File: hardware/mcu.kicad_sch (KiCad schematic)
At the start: 22 parts, among them SW301 RESET, U301 STM32G431

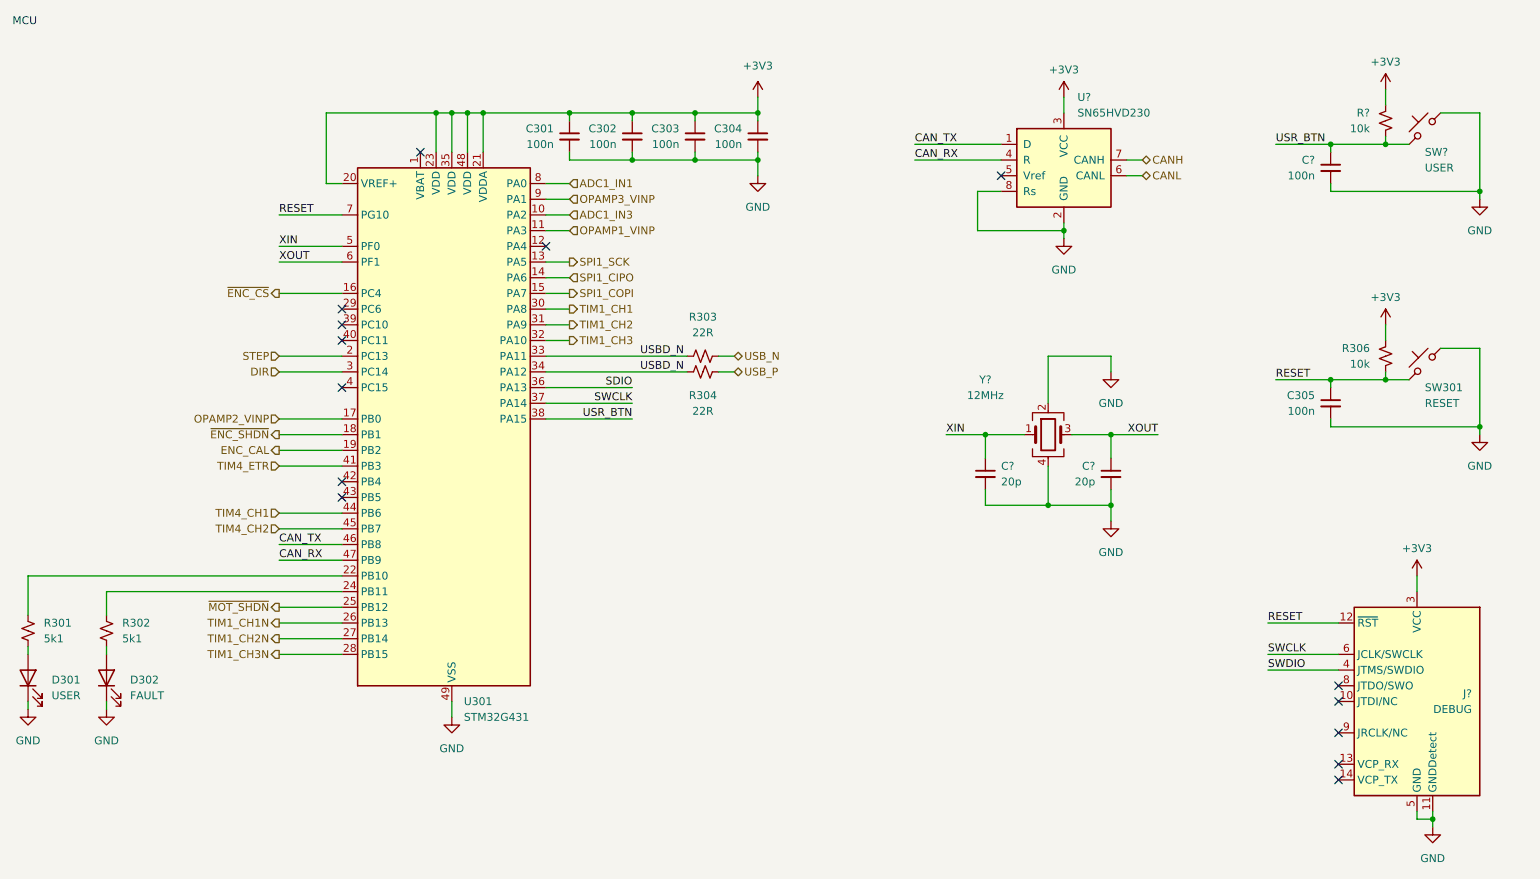
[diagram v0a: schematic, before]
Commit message: finish component selection
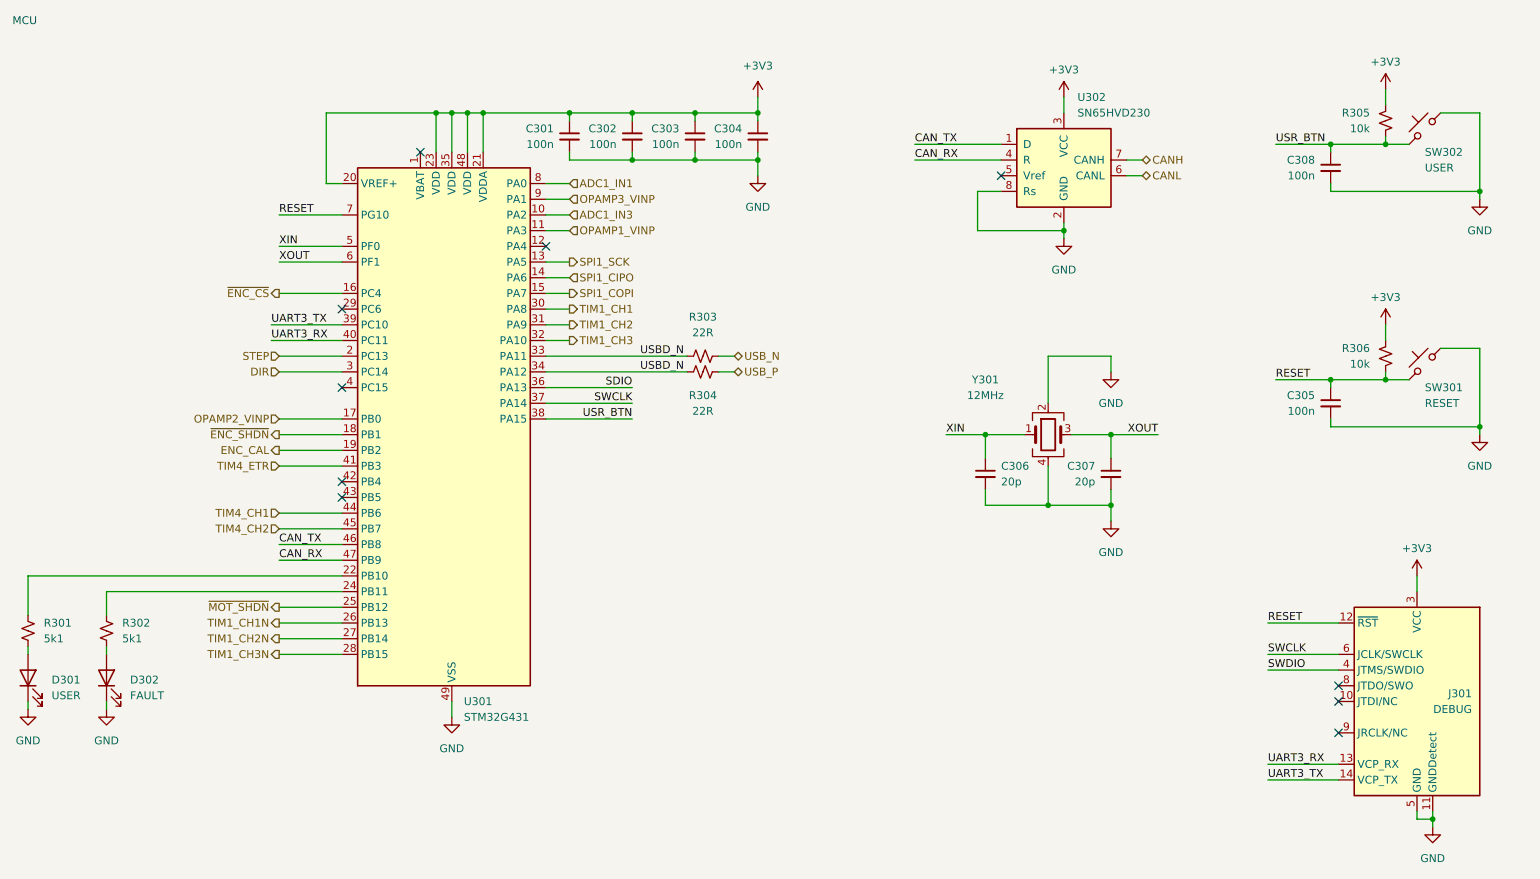
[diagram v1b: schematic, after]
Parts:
- J301: renamed from J?; now left out of the parts list
- gave numbers to parts that had none: 7
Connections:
- net UART3_TX: now reaches U301.39 (PC10)
- net UART3_TX: now also J301.14 (VCP_TX)
- net UART3_RX: now reaches U301.40 (PC11)
- net UART3_RX: now also J301.13 (VCP_RX)
- no-connect marks 14 -> 10

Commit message: try new driver
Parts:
- removed C308: 100n, Capacitor_SMD:C_0402_1005Metric, symbol Device:C_Small
- removed J301: DEBUG, Connector_PinHeader_1.27mm:PinHeader_2x07_P1.27mm_Vertical, symbol Connector:Conn_ST_STDC14
- removed R303, R304: 22R, Resistor_SMD:R_0402_1005Metric, symbol Device:R_Small_US
- removed R305: 10k, Resistor_SMD:R_0402_1005Metric, symbol Device:R_Small_US
- removed SW302: USER, matei:TS-1187A-B-A-B, symbol Switch:SW_Push_45deg
- added J301: TagConnect, Connector:Tag-Connect_TC2030-IDC-NL_2x03_P1.27mm_Vertical, symbol Connector:Conn_ARM_SWD_TagConnect_TC2030-NL
- SW302: renamed from SW301; footprint matei:TS-1187A-B-A-B -> easyeda2kicad:KEY-SMD_4P-L2.6-W1.6-P0.80-LS3.0; LCSC Part C318884 -> C358616
- renumbered C306 to C305, C307 to C306, C305 to C308
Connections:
- net SDIO is gone; now on net SWDIO: U301.36 (PA13)
- net +3V3: now also J301.1 (VCC)
- net GND: now also J301.5 (GND)
- net RESET: now also J301.3 (~{RESET})
- net SWCLK: now also J301.4 (SWCLK)
- net SWDIO: now also J301.2 (SWDIO)
- net USB_N: now also U301.33 (PA11)
- net USB_P: now also U301.34 (PA12)
- net ADC1_IN1: no longer names the net of U301.8 (PA0)
- net ADC1_IN3: no longer names the net of U301.10 (PA2)
- net UART3_RX: no longer names the net of U301.40 (PC11)
- net UART3_TX: no longer names the net of U301.39 (PC10)
- removed net USBD_N: U301.33 (PA11), U301.34 (PA12)
- no-connect marks 10 -> 12

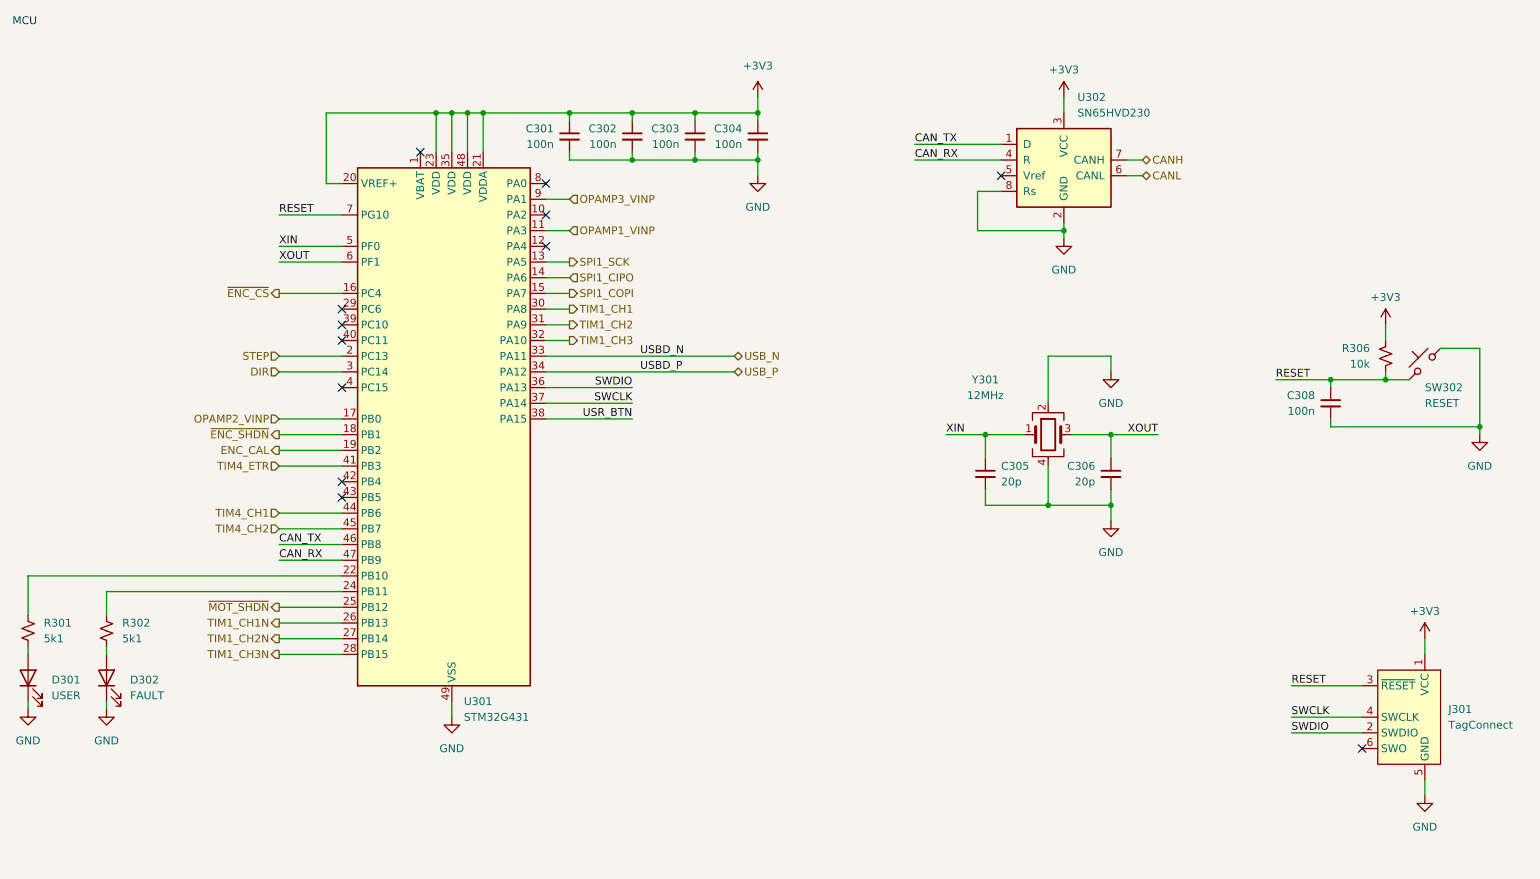
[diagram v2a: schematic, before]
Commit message: change driver configuration
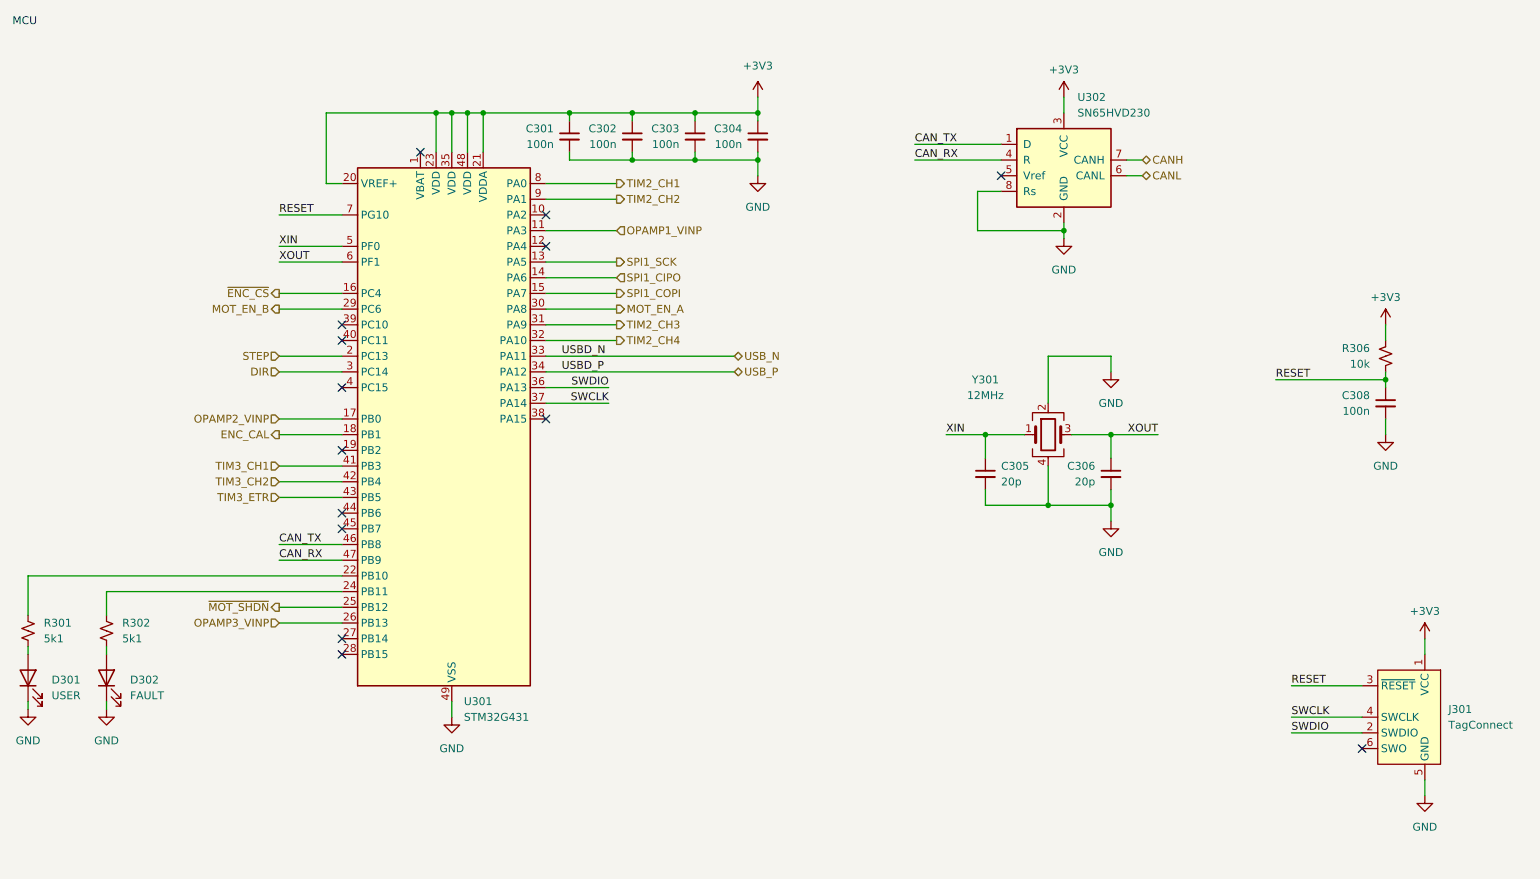
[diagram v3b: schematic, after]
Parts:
- removed SW302: RESET, easyeda2kicad:KEY-SMD_4P-L2.6-W1.6-P0.80-LS3.0, symbol Switch:SW_Push_45deg
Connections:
- net TIM1_CH1N is gone; now on net OPAMP3_VINP: U301.26 (PB13)
- net ~{ENC_SHDN} is gone; now on net ENC_CAL: U301.18 (PB1)
- net ENC_CAL: no longer U301.19 (PB2)
- net OPAMP3_VINP: no longer U301.9 (PA1)
- net MOT_EN_B: now reaches U301.29 (PC6)
- net TIM3_CH2: now reaches U301.42 (PB4)
- net TIM3_ETR: now reaches U301.43 (PB5)
- net TIM2_CH1: now reaches U301.8 (PA0)
- net TIM1_CH1 renamed MOT_EN_A
- net TIM1_CH2 renamed TIM2_CH3
- net TIM1_CH2N: no longer names the net of U301.27 (PB14)
- net TIM1_CH3 renamed TIM2_CH4
- net TIM1_CH3N: no longer names the net of U301.28 (PB15)
- net TIM4_CH1: no longer names the net of U301.44 (PB6)
- net TIM4_CH2: no longer names the net of U301.45 (PB7)
- net TIM4_ETR renamed TIM3_CH1
- net USR_BTN: no longer names the net of U301.38 (PA15)
- new net TIM2_CH2: U301.9 (PA1)
- no-connect marks 12 -> 14
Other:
- moved on the sheet: C308

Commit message: finish layout and prod files
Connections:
- net DIR: now also U301.28 (PB15); no longer U301.3 (PC14)
- net STEP: now also U301.27 (PB14); no longer U301.2 (PC13)
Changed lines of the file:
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@@
   (junction (at 196.85 59.69) (diameter 0) (color 0 0 0 0)
   )
-  (no_connect (at 80.01 128.27))
-  (no_connect (at 80.01 125.73))
   (no_connect (at 80.01 77.47))
   (no_connect (at 245.11 143.51))
@@
   (no_connect (at 113.03 90.17))
   (no_connect (at 113.03 57.15))
+  (no_connect (at 80.01 82.55))
   (no_connect (at 80.01 107.95))
   (no_connect (at 113.03 62.23))
@@
   (no_connect (at 92.71 46.99))
   (no_connect (at 80.01 105.41))
+  (no_connect (at 80.01 80.01))
   (no_connect (at 80.01 85.09))
   (no_connect (at 80.01 95.25))
@@
     (stroke (width 0) (type default))
   )
-  (wire (pts (xy 69.85 80.01) (xy 80.01 80.01))
+  (wire (pts (xy 69.85 125.73) (xy 80.01 125.73))
     (stroke (width 0) (type default))
   )
@@
     (stroke (width 0) (type default))
   )
-  (wire (pts (xy 69.85 82.55) (xy 80.01 82.55))
+  (wire (pts (xy 69.85 128.27) (xy 80.01 128.27))
     (stroke (width 0) (type default))
   )
@@
     (stroke (width 0) (type default))
   )
-  (image (at 11.43 74.93) (scale 0.819139)
+  (image (at -36.83 85.09) (scale 0.819139)
     (data
       iVBORw0KGgoAAAANSUhEUgAABGYAAARCCAIAAABuFmOEAAAAA3NCSVQICAjb4U/gAAAACXBIWXMA
@@
     (effects (font (size 1.27 1.27)) (justify left))
   )
-  (hierarchical_label "STEP" (shape input) (at 69.85 80.01 180) (fields_autoplaced)
+  (hierarchical_label "STEP" (shape input) (at 69.85 125.73 180) (fields_autoplaced)
     (effects (font (size 1.27 1.27)) (justify right))
   )
@@
     (effects (font (size 1.27 1.27)) (justify right))
   )
-  (hierarchical_label "DIR" (shape input) (at 69.85 82.55 180) (fields_autoplaced)
+  (hierarchical_label "DIR" (shape input) (at 69.85 128.27 180) (fields_autoplaced)
     (effects (font (size 1.27 1.27)) (justify right))
   )

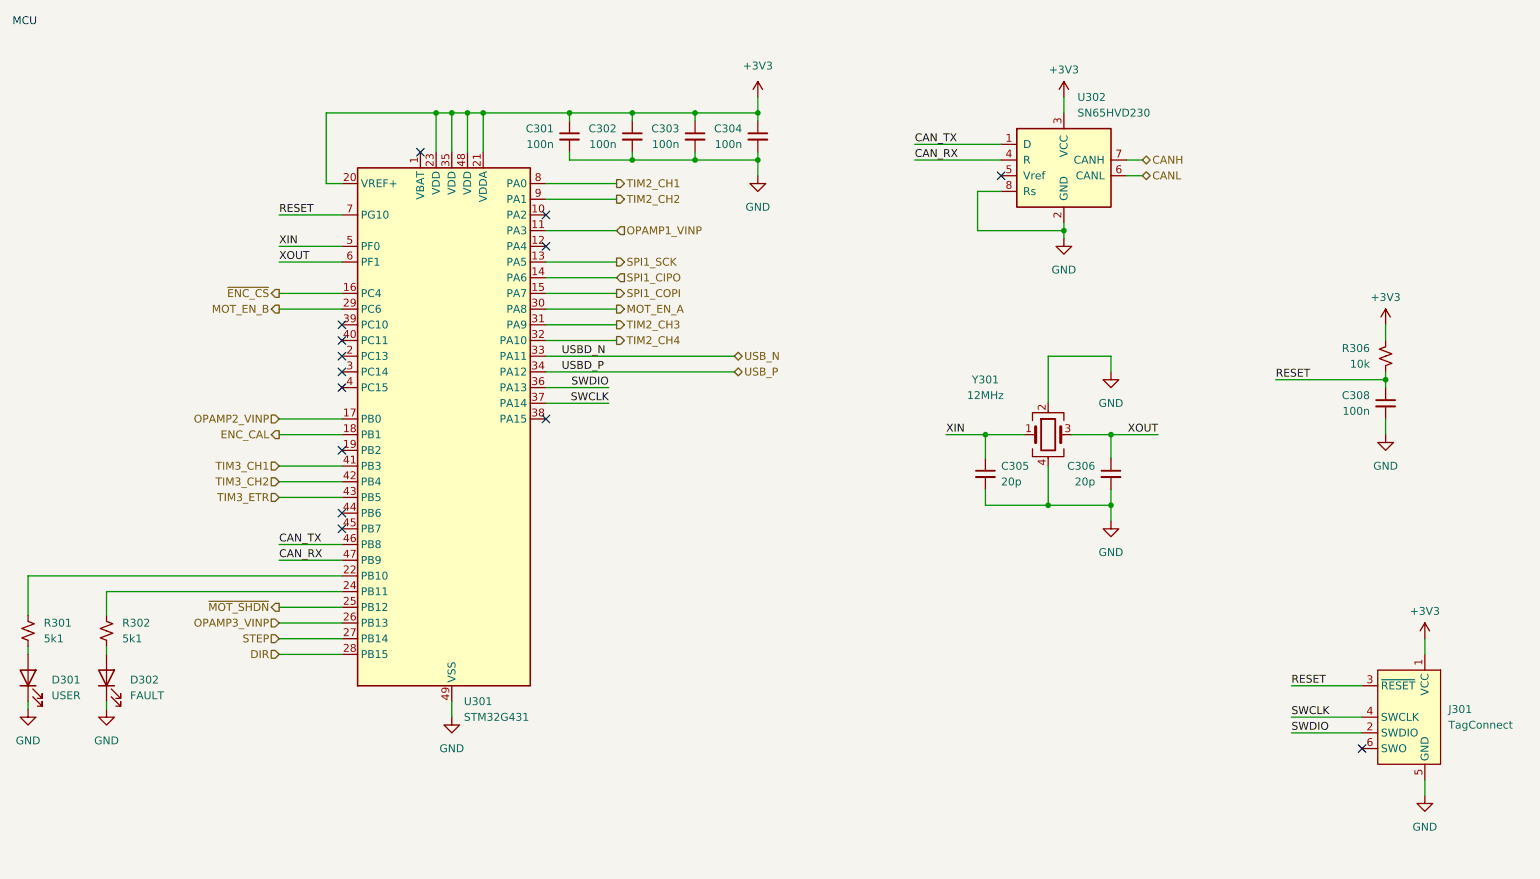
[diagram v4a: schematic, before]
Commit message: work on analog layout
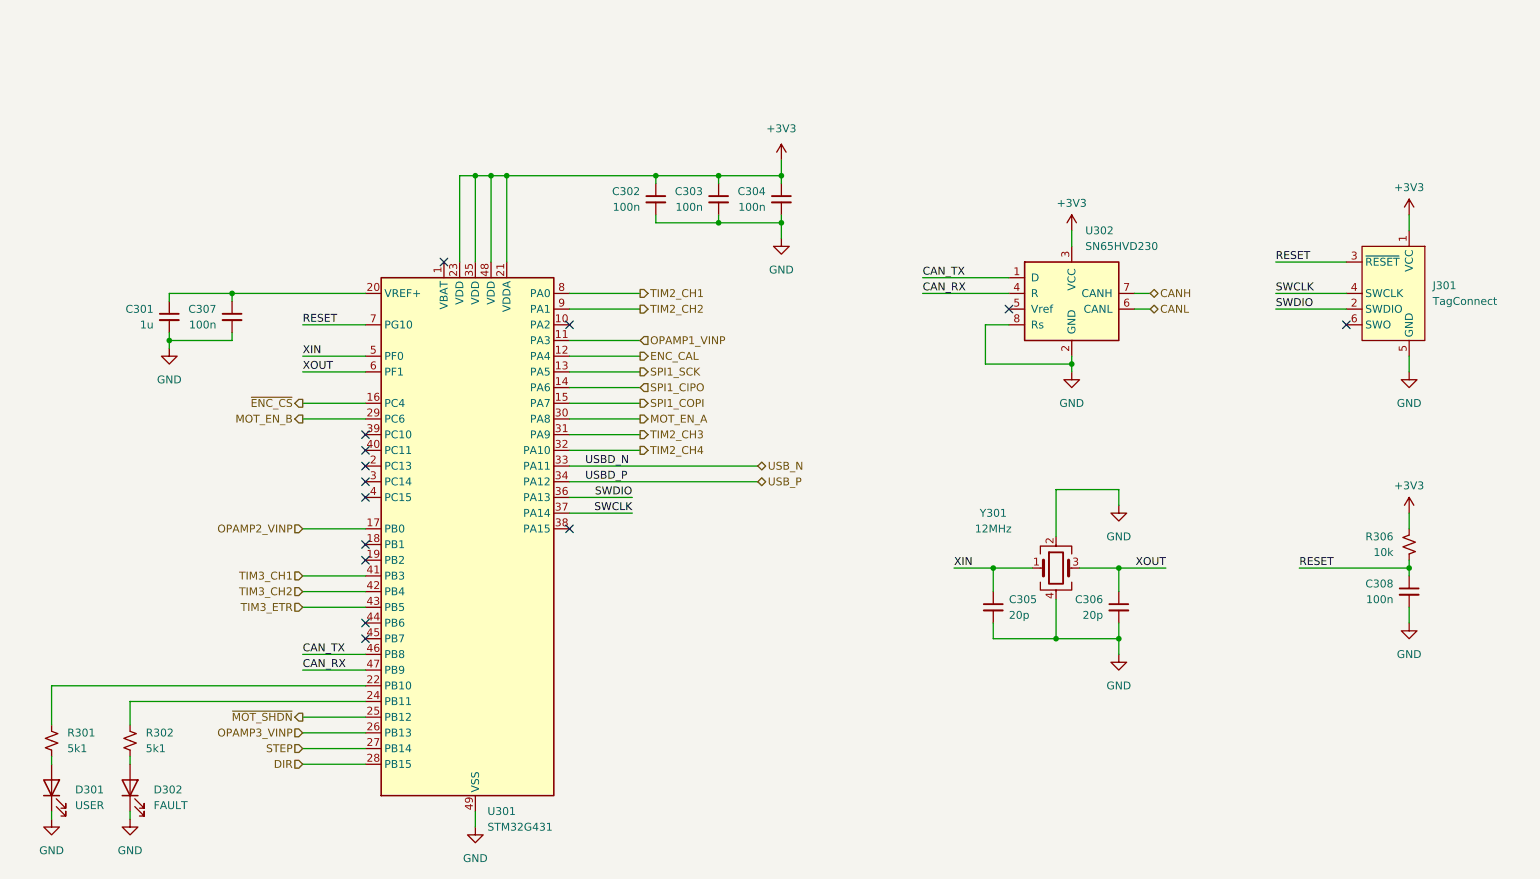
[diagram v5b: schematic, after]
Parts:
- added C307: 100n, Capacitor_SMD:C_0402_1005Metric, symbol Device:C_Small
- C301: value 100n -> 1u; LCSC Part C307331 -> C52923
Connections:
- net +3V3: no longer C301.1, U301.20 (VREF+)
- net ENC_CAL: now also U301.12 (PA4); no longer U301.18 (PB1)
- net GND: now also C307.2
- new net: C301.1, C307.1, U301.20 (VREF+)
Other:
- note removed: "MCU"
- moved on the sheet: C302, C303, C304, C305, C306, C308, D301, D302, J301, R301, R302, R306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
